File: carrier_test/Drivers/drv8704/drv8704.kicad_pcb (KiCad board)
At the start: 2 copper layers, 28 parts, among them IC1 DRV8704, IC2 MP8759, Q1 SiZ340DT, Q2 SiZ340DT, Q3 SiZ340DT, Q4 SiZ340DT

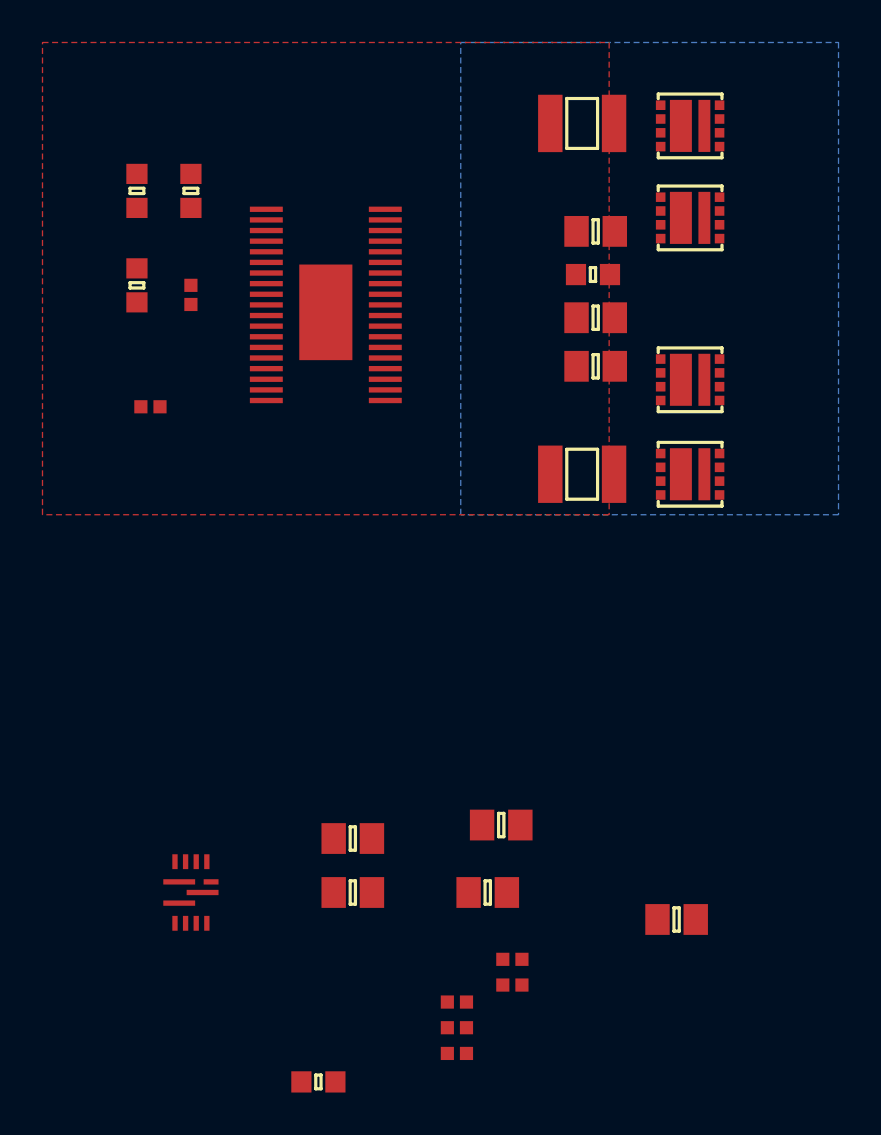
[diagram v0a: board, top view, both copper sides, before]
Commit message: [UNAV2] - initial draft of drv8704 based driver
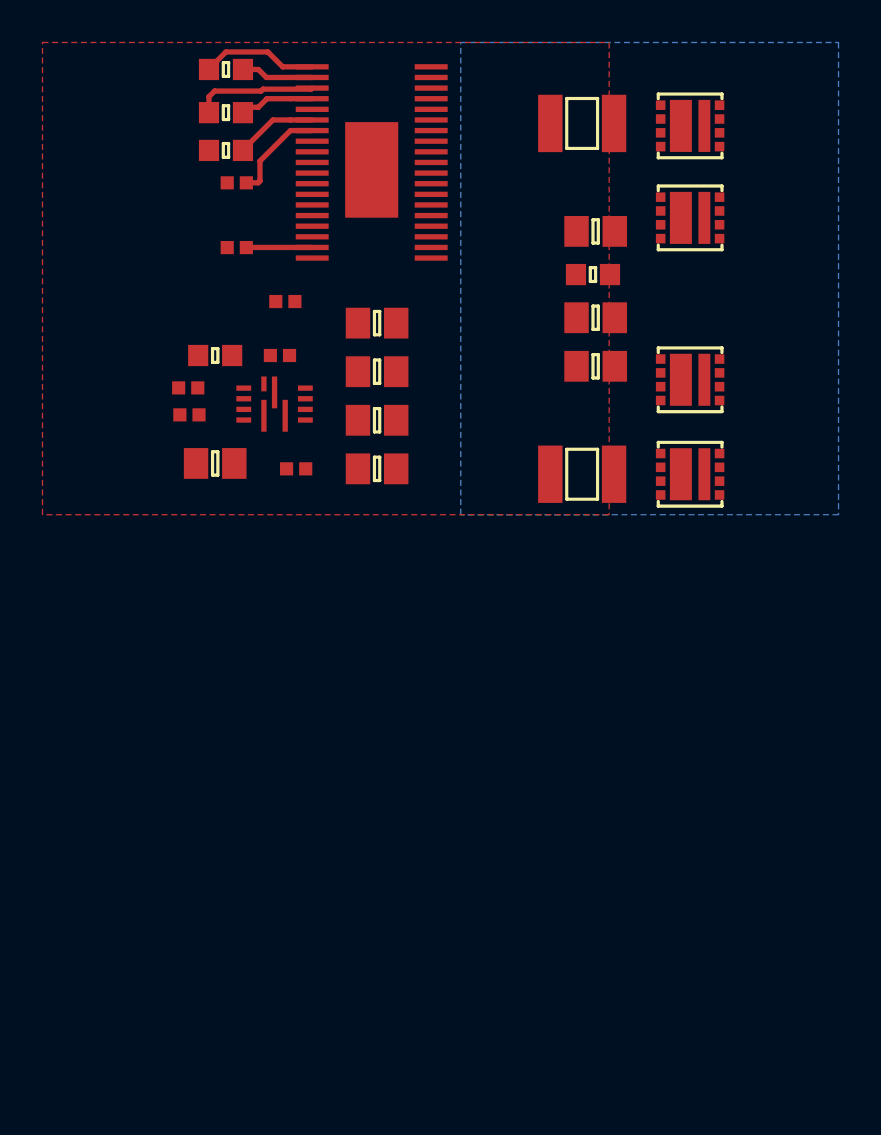
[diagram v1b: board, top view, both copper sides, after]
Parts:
- moved C10 34.5 mm to (69.1, 89.7), turned to 180 degrees
- moved R7 33.9 mm to (72.4, 87.1), turned to 180 degrees
- moved R6 32.7 mm to (67.8, 91.2)
- moved R8 32.6 mm to (67.9, 92.5), turned to 180 degrees
- moved R4 31.5 mm to (72.1, 89.7)
- moved C9 30.5 mm to (69.1, 94.7), turned to 180 degrees
- moved C15 26.8 mm to (76.7, 88.1), turned to 180 degrees
- moved R5 25.2 mm to (72.9, 95.0)
- moved IC2 23.3 mm to (71.9, 91.9), turned to 90 degrees
- moved C14 22.8 mm to (76.7, 92.7), turned to 180 degrees
- moved C16 22.1 mm to (76.7, 90.4), turned to 180 degrees
- moved C13 17.4 mm to (76.7, 95.0), turned to 180 degrees
- moved R1 8.52 mm to (70.1, 84.6)
- moved C6 7.61 mm to (69.6, 80.0), turned to 180 degrees
- moved IC1 7.04 mm to (76.5, 81.0)
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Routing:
- net Net-(C8-Pad1): track 0.00 -> 5.78 mm
- net Net-(C7-Pad1): track 0.00 -> 5.50 mm
- net Net-(C4-Pad2): track 0.00 -> 4.67 mm
- net Net-(C6-Pad1): track 0.00 -> 3.87 mm
- net /Driver/VMOT: track 0.00 -> 3.42 mm
- net Net-(C7-Pad2): track 0.00 -> 3.41 mm
- net /Driver/FAULTn: track 0.00 -> 3.10 mm
